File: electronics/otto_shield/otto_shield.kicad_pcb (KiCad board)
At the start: 2 copper layers, 72.4 x 135.9 mm, 9 parts, among them J1 right_encoder, J2 left_encoder, U1 az_serial_module

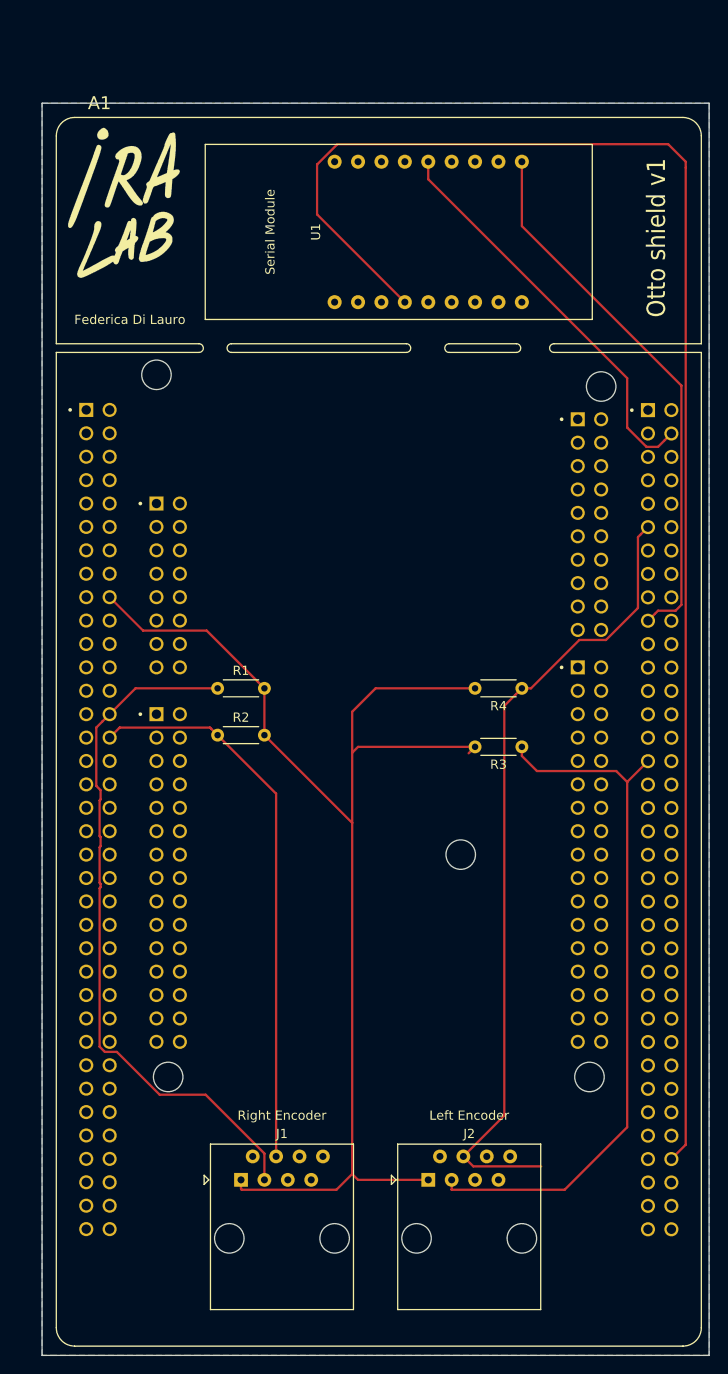
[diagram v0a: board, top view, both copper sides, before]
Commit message: change rj45 connector to shielded rj45
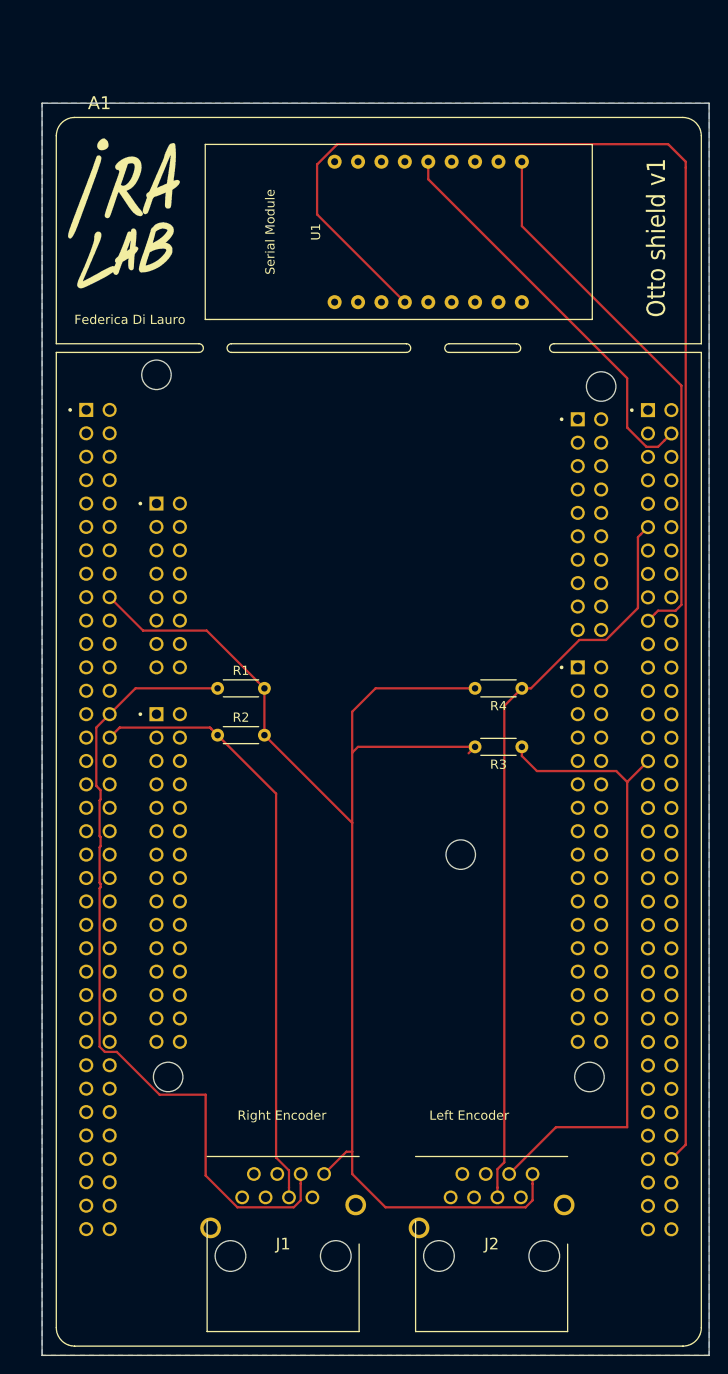
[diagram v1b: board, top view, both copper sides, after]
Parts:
- J1: value right_encoder -> 3-5338556-1; footprint Connector_RJ:RJ45_Amphenol_54602-x08_Horizontal -> rj45-353385561:353385561
- J2: footprint Connector_RJ:RJ45_Amphenol_54602-x08_Horizontal -> rj45-353385561:353385561
- moved J2 11.3 mm to (144.7, 149.2)
- moved J1 9.04 mm to (122.0, 149.2)
- moved G*** 1.14 mm to (100.3, 45.0)
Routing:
- net Net-(A1-PadCN11_28): track 75.5 -> 87.3 mm
- net Net-(A1-PadCN12_31): track 77.2 -> 69.2 mm
- net Net-(A1-PadCN12_11): track 87.8 -> 81.8 mm
- net Net-(A1-PadCN11_18): track 140.9 -> 146.9 mm
- net Net-(A1-PadCN11_30): track 60.9 -> 65.9 mm

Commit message: add connection from the serial module to allow reset
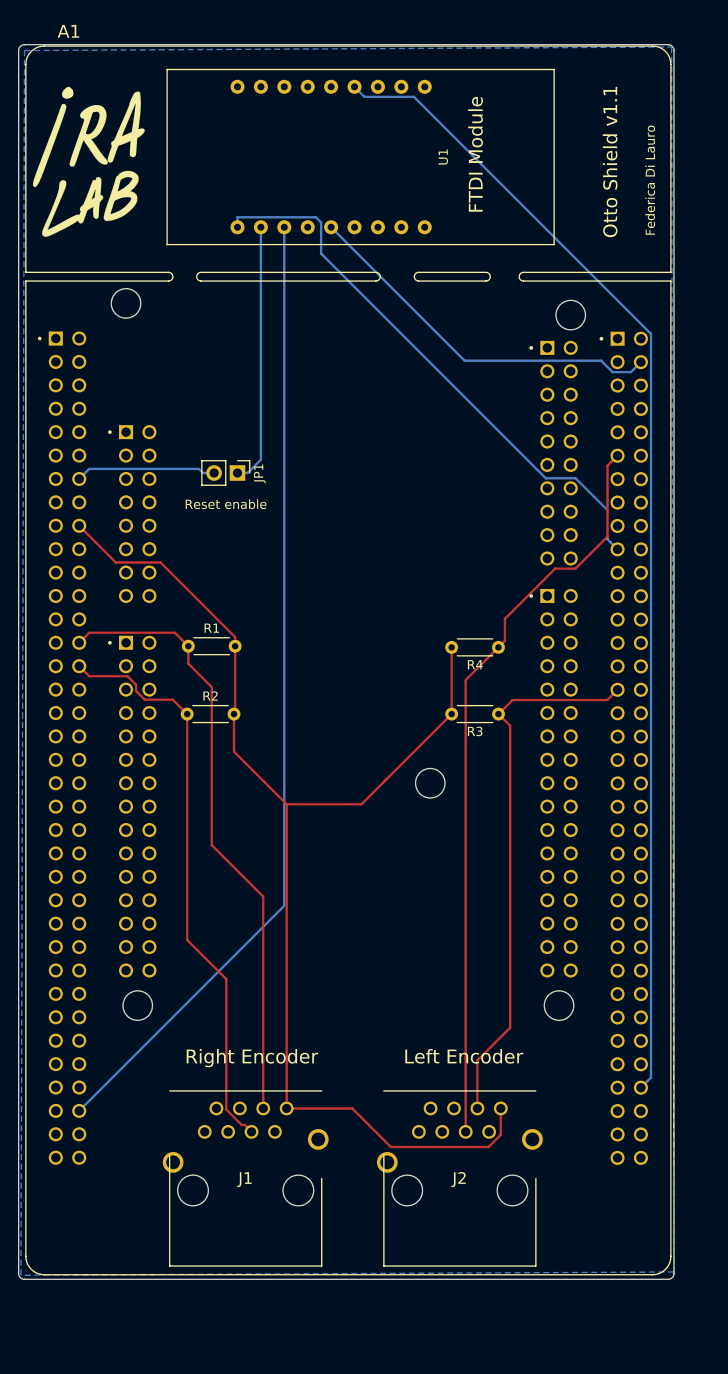
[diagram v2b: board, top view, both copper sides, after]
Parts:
- added JP1: Jumper, Connector_PinHeader_2.54mm:PinHeader_1x02_P2.54mm_Vertical, F.Cu at (112.6, 73.2)
- J2: value left_encoder -> 3-5338556-1
- moved U1 16.9 mm to (135.5, 38.9), turned to 270 degrees
- moved A1 8.42 mm to (124.7, 93.5)
- moved J1 8.19 mm to (118.0, 142.1)
- moved J2 7.90 mm to (141.2, 142.1)
- moved G*** 6.76 mm to (96.5, 39.4)
- moved R1 5.57 mm to (107.3, 91.9)
- moved R4 5.12 mm to (141.0, 92.1)
- moved R3 4.37 mm to (141.0, 99.3)
- moved R2 4.02 mm to (107.2, 99.3)
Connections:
- net Net-(A1-PadCN11_18) renamed +5V
- net Net-(A1-PadCN11_28) renamed /TIM5_CH1
- net Net-(A1-PadCN11_30) renamed /TIM5_CH2
- net Net-(A1-PadCN12_11) renamed /TIM2_CH1
- net Net-(A1-PadCN12_19) renamed /USART_RX
- net Net-(A1-PadCN12_31) renamed /TIM2_CH2
- net Net-(A1-PadCN12_4) renamed /USART_TX
- net Net-(A1-PadCN12_66) renamed /USART_RTS
- A1 pad CN11_14: (no net) -> /RESET
- A1 pad CN11_68: (no net) -> /USART_CTS
- U1 pad 16: (no net) -> /USART_CTS
- U1 pad 17: (no net) -> Net-(JP1-Pad1)
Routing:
- net /USART_CTS: track 0.00 -> 105.1 mm
- net /USART_RTS: track 169.5 -> 125.5 mm
- net Net-(JP1-Pad1): track 0.00 -> 28.4 mm
- net /TIM5_CH1: track 87.3 -> 66.4 mm
- net /RESET: track 0.00 -> 15.3 mm
- net +5V: track 146.9 -> 133.5 mm
- net /TIM2_CH2: track 69.2 -> 58.8 mm
- net /USART_TX: track 44.1 -> 40.6 mm
- net /TIM5_CH2: track 65.9 -> 62.7 mm
- net /USART_RX: track 59.6 -> 61.1 mm
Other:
- board size 72.4 x 135.9 mm -> 71.1 x 134 mm
- board text added: "FTDI Module"
- board text added: "Otto Shield v1.1"
- board text added: "Reset enable"
- board text removed: "Otto shield v1"
- board text removed: "Serial Module"
